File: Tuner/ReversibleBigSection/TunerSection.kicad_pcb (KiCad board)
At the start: 2 copper layers, 100 x 100 mm, 118 parts, among them J1 Conn_01x03, J10 Conn_01x02, J11 Conn_02x05_Odd_Even, J12 Conn_01x01, J13 Conn_01x01, J14 Conn_01x01, J15 Conn_01x01, J16 Conn_01x01, J17 Conn_01x01, J18 Conn_01x01, J19 Conn_01x01, J2 Conn_01x03, J20 Conn_01x01, J21 Conn_01x01, J22 Conn_01x01, J3 Conn_01x03, J4 Conn_01x03, J5 Conn_01x03, J6 Conn_01x03, J7 Conn_01x03, J8 Conn_01x02, J9 Conn_01x02, P10 Conn_01x01, P11 Conn_01x01, P12 Conn_01x01, P2 Conn_01x01, P3 Conn_01x01, P4 Conn_01x01, P5 Conn_01x01, P6 Conn_01x01, P7 Conn_01x01, P8 Conn_01x01, P9 Conn_01x01, U1 MCP23008, U2 ULN2803A

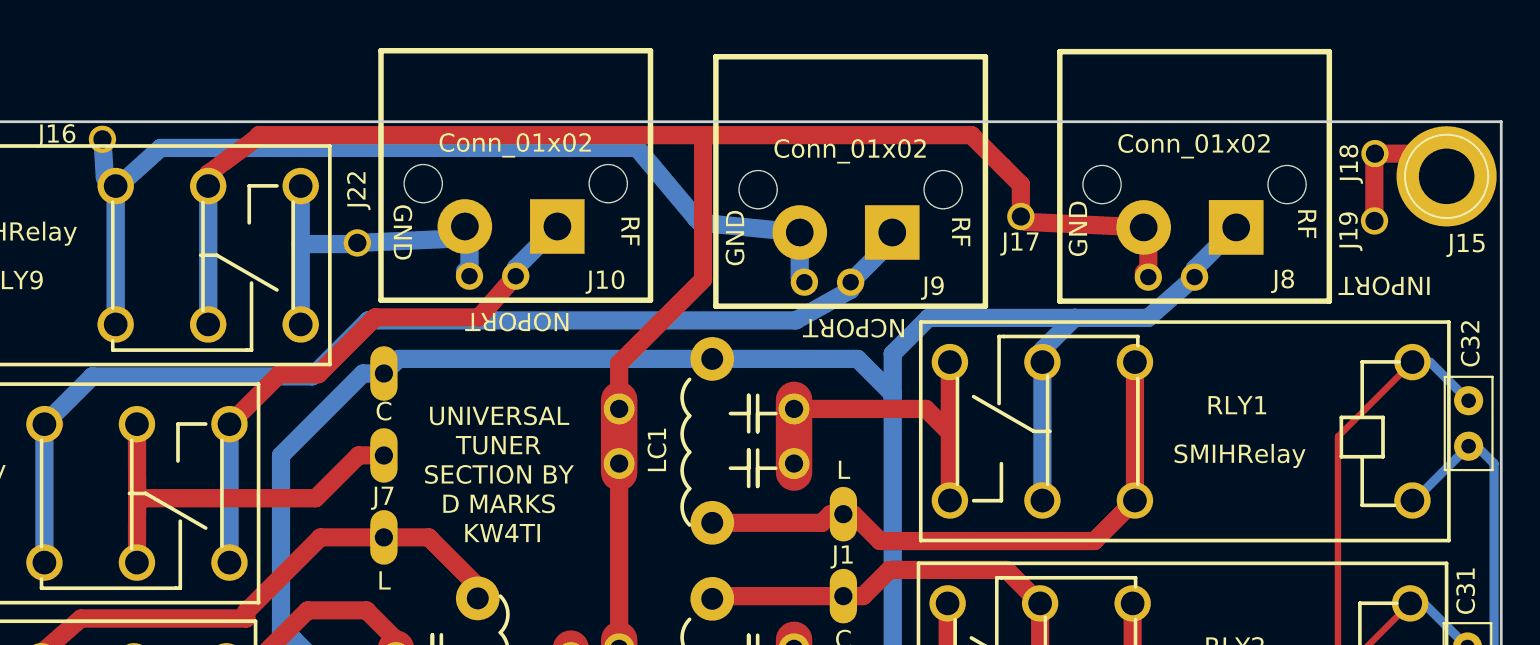
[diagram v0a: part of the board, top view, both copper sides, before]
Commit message: Added nonswitched output to ReversibleSections
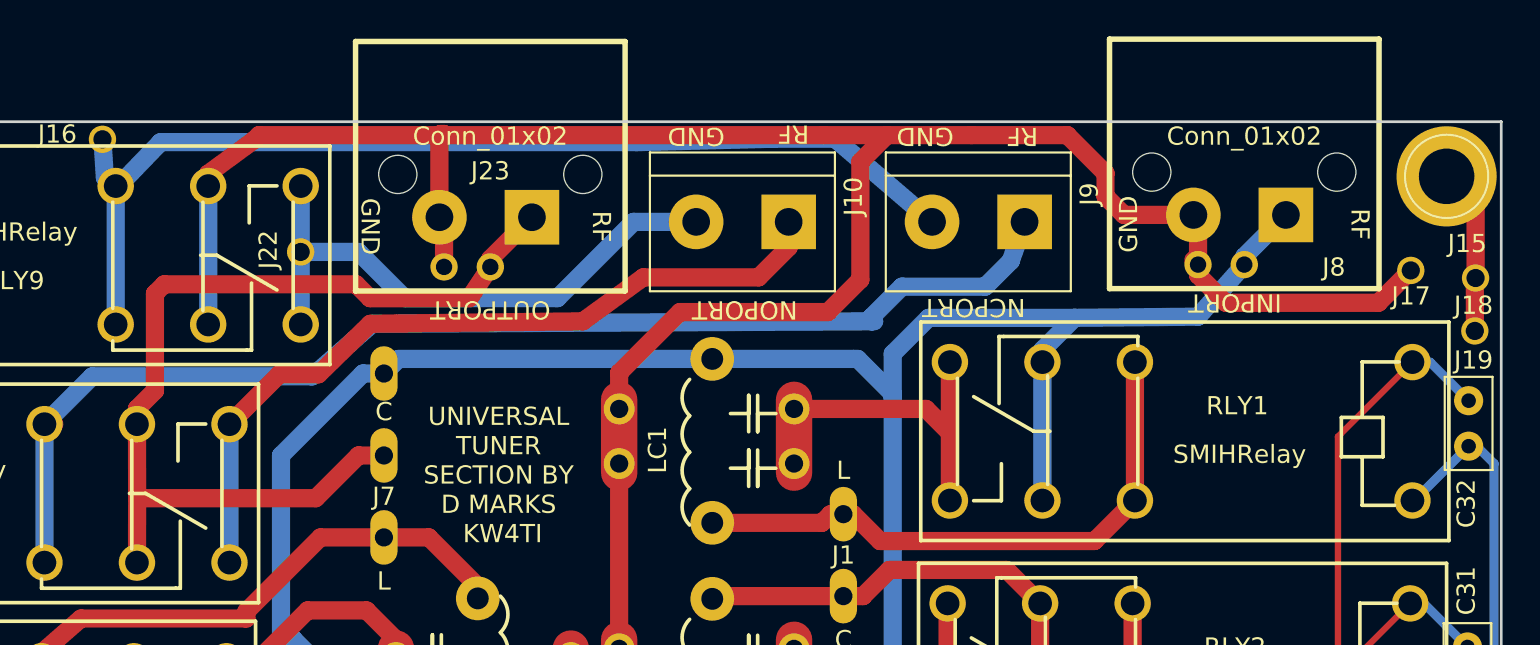
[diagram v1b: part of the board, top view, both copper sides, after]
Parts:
- added J23: Conn_01x02, tuner:bnc_90_1-1337543-0_pad_combo, F.Cu at (94.5, 45.6)
- J10, J9: footprint tuner:bnc_90_1-1337543-0_pad_combo -> Connectors_Terminal_Blocks:TerminalBlock_bornier-2_P5.08mm
- moved J17 21.6 mm to (146.3, 58.2)
- moved J10 17.7 mm to (110.9, 55.5)
- moved J9 13.2 mm to (123.8, 55.5)
- moved J18 8.78 mm to (147.3, 58.6)
- moved J19 8.18 mm to (147.3, 61.5)
- moved J22 3.15 mm to (85.3, 57.1)
- moved J8 2.82 mm to (135.9, 45.5)
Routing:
- net RFGND: track 147.0 -> 181.0 mm
- net Net-(J23-Pad1): track 22.1 -> 53.2 mm
- net Net-(J10-Pad1): track 30.7 -> 43.7 mm
- net Net-(J10-Pad2): track 20.1 -> 32.1 mm
- net Net-(J9-Pad1): track 59.3 -> 67.7 mm
- net Net-(J16-Pad1): track 53.6 -> 58.0 mm
- net RFPORT1: track 168.9 -> 172.1 mm
- net Net-(J15-Pad1): track 9.87 -> 12.6 mm
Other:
- board text added: "OUTPORT"

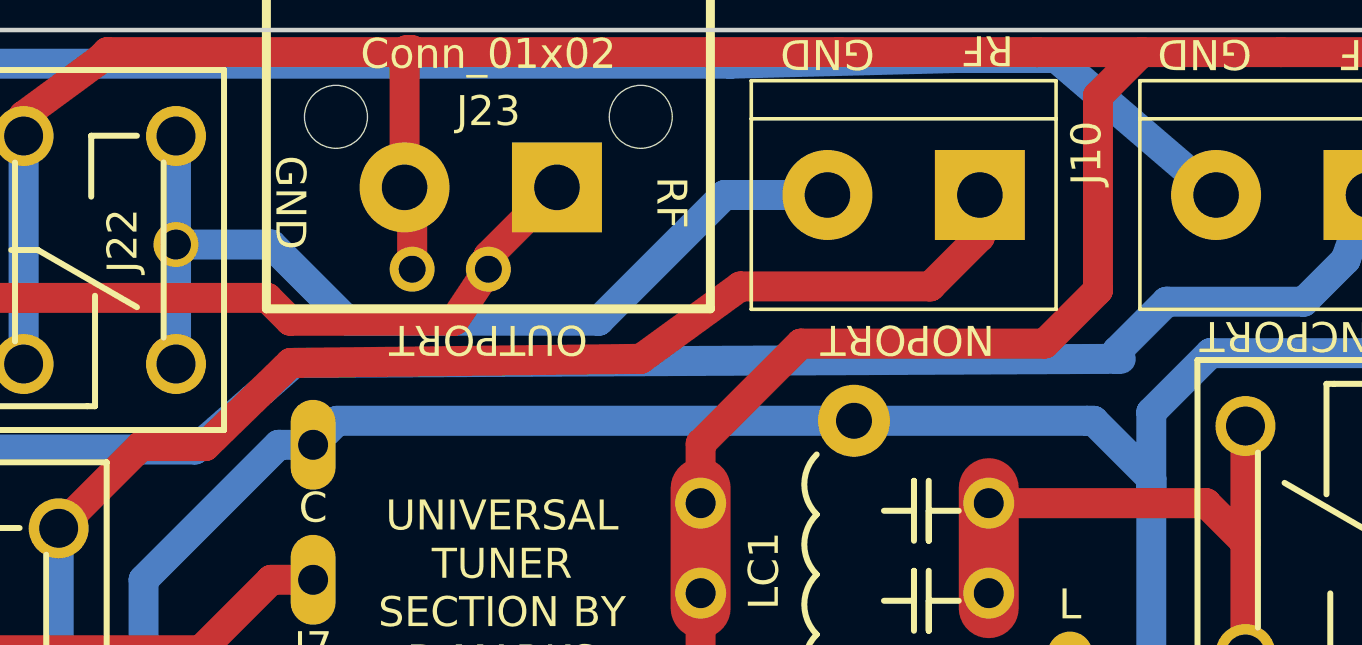
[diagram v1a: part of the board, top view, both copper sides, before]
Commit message: Change named to DirectionalCoupler, fixed order of two pins in QuadCoupler
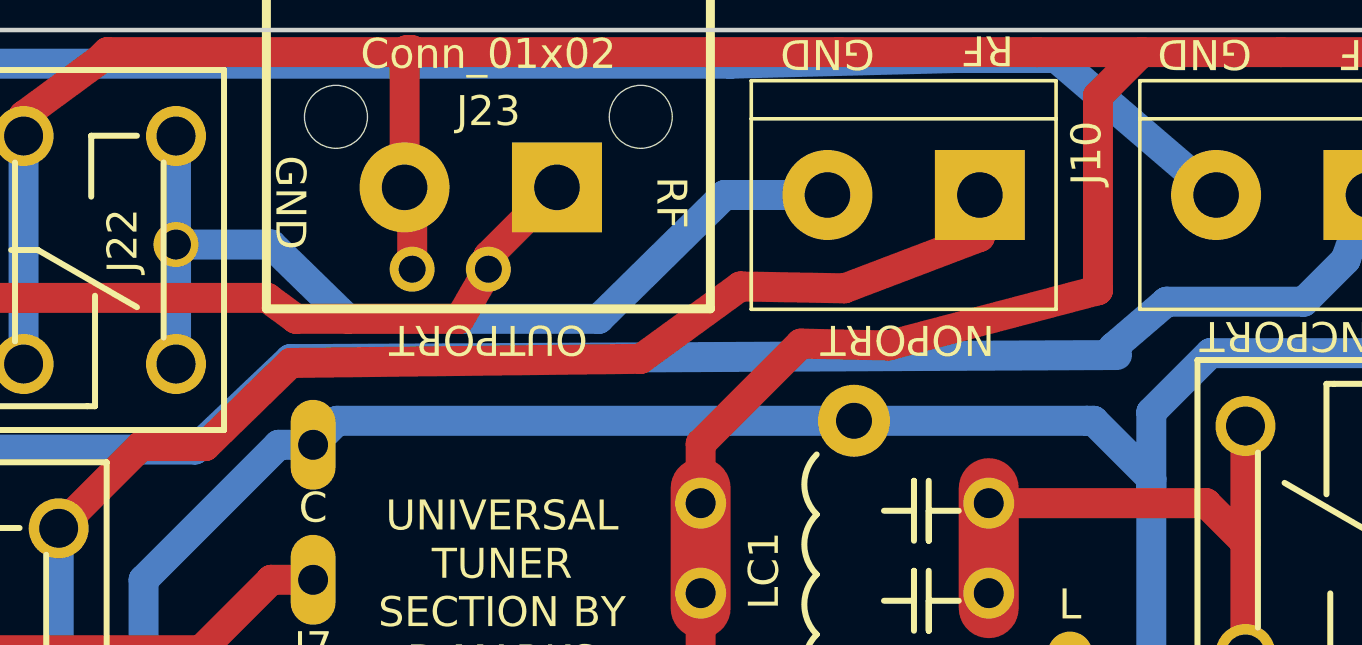
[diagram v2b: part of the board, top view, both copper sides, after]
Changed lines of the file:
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@@
   (segment (start 114.808 52.197) (end 116.2685 50.7365) (width 1) (layer F.Cu) (net 1))
   (segment (start 114.808 58.674) (end 114.808 52.197) (width 1) (layer F.Cu) (net 1))
-  (segment (start 113.03 60.452) (end 114.808 58.674) (width 1) (layer F.Cu) (net 1))
-  (segment (start 104.902 60.452) (end 113.03 60.452) (width 1) (layer F.Cu) (net 1))
+  (segment (start 107.823 60.5155) (end 114.808 58.674) (width 1) (layer F.Cu) (net 1))
+  (segment (start 104.902 60.452) (end 107.823 60.5155) (width 1) (layer F.Cu) (net 1))
   (segment (start 101.564 63.79) (end 104.902 60.452) (width 1) (layer F.Cu) (net 1))
   (segment (start 91.948 57.973) (end 91.948 55.499) (width 1) (layer F.Cu) (net 1) (status 30))
@@
   (segment (start 79.99728 79.62884) (end 79.99728 87.22884) (width 1) (layer B.Cu) (net 21) (status 30))
   (segment (start 110.871 55.499) (end 110.871 56.896) (width 1) (layer F.Cu) (net 22) (status 30))
-  (segment (start 110.871 56.896) (end 109.22 58.547) (width 1) (layer F.Cu) (net 22) (status 10))
-  (segment (start 109.22 58.547) (end 102.886379 58.547) (width 1) (layer F.Cu) (net 22))
+  (segment (start 110.871 56.896) (end 106.3625 58.6105) (width 1) (layer F.Cu) (net 22) (status 10))
+  (segment (start 106.3625 58.6105) (end 102.886379 58.547) (width 1) (layer F.Cu) (net 22))
   (segment (start 99.568 60.96) (end 87.895029 61.09832) (width 1) (layer F.Cu) (net 22))
   (segment (start 87.895029 61.09832) (end 85.0519 63.8683) (width 1) (layer F.Cu) (net 22))
@@
   (segment (start 80.16492 66.6088) (end 80.16492 66.3863) (width 1) (layer B.Cu) (net 22) (status 30))
   (segment (start 80.16492 66.6088) (end 80.16492 74.2088) (width 1) (layer B.Cu) (net 22) (status 30))
-  (segment (start 115.443003 60.960631) (end 115.443003 60.705997) (width 1) (layer B.Cu) (net 23))
+  (segment (start 115.316003 60.833631) (end 115.316003 60.578997) (width 1) (layer B.Cu) (net 23))
   (segment (start 123.063 57.658) (end 123.825 55.499) (width 1) (layer B.Cu) (net 23) (status 20))
   (segment (start 121.666 59.055) (end 123.063 57.658) (width 1) (layer B.Cu) (net 23))
   (segment (start 117.094 59.055) (end 121.666 59.055) (width 1) (layer B.Cu) (net 23))
-  (segment (start 115.443003 60.705997) (end 117.094 59.055) (width 1) (layer B.Cu) (net 23))
-  (segment (start 115.57 60.96) (end 115.443003 60.960631) (width 1) (layer B.Cu) (net 23))
-  (segment (start 115.443003 60.960631) (end 88.009613 61.096962) (width 1) (layer B.Cu) (net 23))
+  (segment (start 115.316003 60.578997) (end 117.094 59.055) (width 1) (layer B.Cu) (net 23))
+  (segment (start 115.443 60.833) (end 115.316003 60.833631) (width 1) (layer B.Cu) (net 23))
+  (segment (start 115.316003 60.833631) (end 87.882613 60.969962) (width 1) (layer B.Cu) (net 23))
   (segment (start 70.00492 66.6088) (end 70.00492 74.2088) (width 1) (layer B.Cu) (net 23))
   (segment (start 72.63112 63.9826) (end 70.00492 66.6088) (width 1) (layer B.Cu) (net 23))
   (segment (start 84.709 63.9826) (end 72.63112 63.9826) (width 1) (layer B.Cu) (net 23))
-  (segment (start 88.009613 61.096962) (end 84.709 63.9826) (width 1) (layer B.Cu) (net 23))
+  (segment (start 87.882613 60.969962) (end 84.709 63.9826) (width 1) (layer B.Cu) (net 23))
   (segment (start 123.19 55.118) (end 123.19 55.56) (width 1) (layer B.Cu) (net 23) (status 30))
   (segment (start 70.00492 66.6088) (end 70.54442 66.6088) (width 1) (layer F.Cu) (net 23) (status 30))
@@
   (segment (start 84.074 57.15) (end 87.249 57.15) (width 1) (layer B.Cu) (net 38))
   (segment (start 102.362 55.499) (end 105.791 55.499) (width 1) (layer B.Cu) (net 38) (status 20))
-  (segment (start 98.171 59.69) (end 102.362 55.499) (width 1) (layer B.Cu) (net 38))
-  (segment (start 89.789 59.69) (end 98.171 59.69) (width 1) (layer B.Cu) (net 38))
-  (segment (start 87.249 57.15) (end 89.789 59.69) (width 1) (layer B.Cu) (net 38))
+  (segment (start 98.171 59.6265) (end 102.362 55.499) (width 1) (layer B.Cu) (net 38))
+  (segment (start 89.789 59.6265) (end 98.171 59.6265) (width 1) (layer B.Cu) (net 38))
+  (segment (start 87.249 57.15) (end 89.789 59.6265) (width 1) (layer B.Cu) (net 38))
   (segment (start 84.074 57.15) (end 84.074 53.5354) (width 1) (layer B.Cu) (net 38))
   (segment (start 84.074 53.5354) (end 84.07652 53.53288) (width 1) (layer B.Cu) (net 38))
@@
   (segment (start 75.08492 66.6088) (end 75.08492 65.75808) (width 1) (layer F.Cu) (net 74))
   (segment (start 75.08492 65.75808) (end 76.073 64.77) (width 1) (layer F.Cu) (net 74))
-  (segment (start 93.345 59.69) (end 94.488 57.973) (width 1) (layer F.Cu) (net 74) (status 20))
-  (segment (start 87.884 59.69) (end 93.345 59.69) (width 1) (layer F.Cu) (net 74))
-  (segment (start 87.122 58.928) (end 87.884 59.69) (width 1) (layer F.Cu) (net 74))
+  (segment (start 93.5355 59.6265) (end 94.488 57.973) (width 1) (layer F.Cu) (net 74) (status 20))
+  (segment (start 88.0745 59.6265) (end 93.5355 59.6265) (width 1) (layer F.Cu) (net 74))
+  (segment (start 87.122 58.928) (end 88.0745 59.6265) (width 1) (layer F.Cu) (net 74))
   (segment (start 76.581 58.928) (end 87.122 58.928) (width 1) (layer F.Cu) (net 74))
   (segment (start 76.073 59.436) (end 76.581 58.928) (width 1) (layer F.Cu) (net 74))

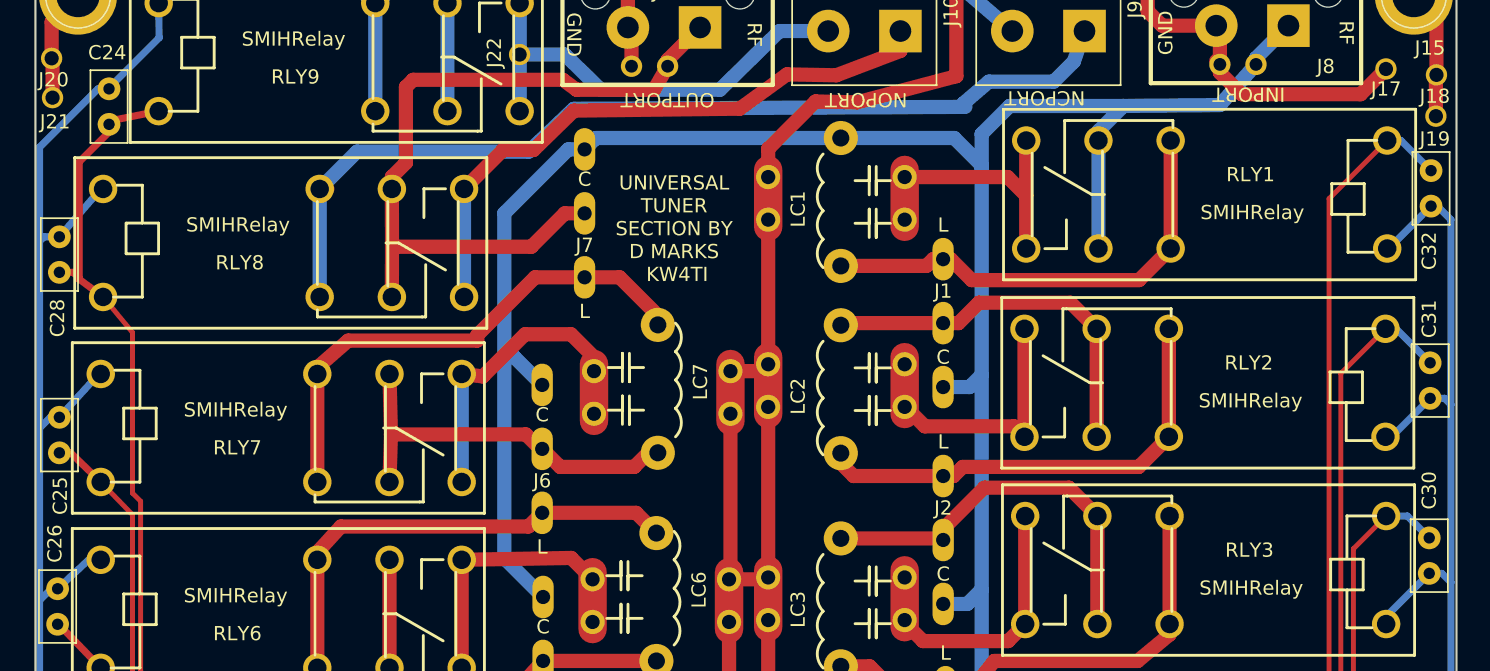
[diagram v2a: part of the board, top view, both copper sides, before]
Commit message: Added extra capacitors between relay power and ground posts
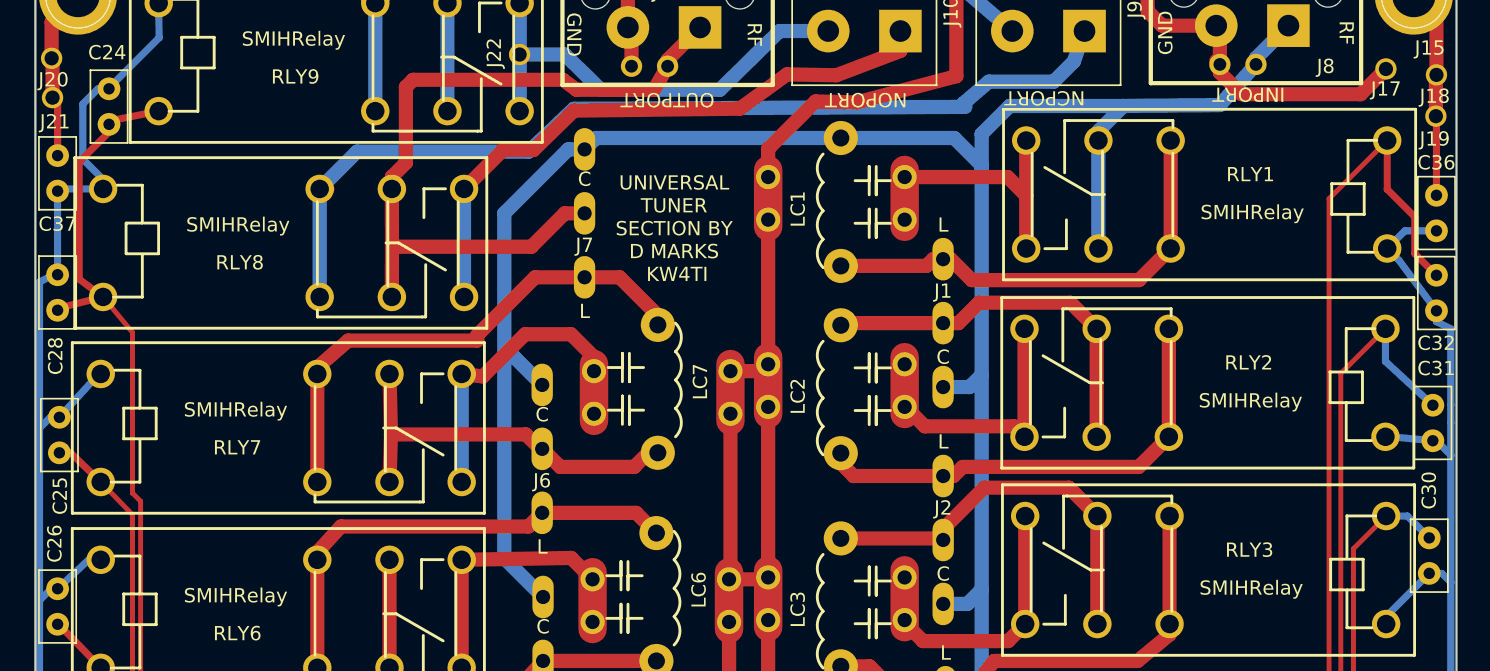
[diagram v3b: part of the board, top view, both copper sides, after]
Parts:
- added C36: 10 nF, Capacitors_THT:C_Disc_D5.0mm_W2.5mm_P2.50mm, F.Cu at (148.6, 67.1)
- added C37: 10 nF, Capacitors_THT:C_Disc_D5.0mm_W2.5mm_P2.50mm, F.Cu at (51.6, 64.3)
- moved C32 7.38 mm to (148.6, 75.2)
- moved C31 2.99 mm to (148.3, 84.3)
- moved C28 2.67 mm to (51.6, 72.6)
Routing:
- net RLY1: track 120.2 -> 127.7 mm
- net Net-(C36-Pad1): track 12.6 -> 18.2 mm
- net RLYPWR: track 358.3 -> 353.9 mm
- net Net-(C37-Pad1): track 9.57 -> 13.8 mm
- net RLY2: track 96.8 -> 99.5 mm
- net RLY8: track 164.8 -> 166.5 mm
